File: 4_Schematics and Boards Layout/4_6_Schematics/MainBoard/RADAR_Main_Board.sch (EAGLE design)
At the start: 791 parts, among them IC1 AT93C46A-10SQ-2.7, J1 142-0731-211, J18 142-0731-211, J19 CJT-T-P-HH-ST-TH1, J20 142-0731-211, J21 CJT-T-P-HH-ST-TH1, J22 142-0731-211, J23 142-0731-211, J24 142-0731-211, J25 142-0731-211, J26 142-0731-211, J27 142-0731-211, J28 142-0731-211, J29 142-0731-211, J30 142-0731-211, J31 142-0731-211, J32 142-0731-211, J33 142-0731-211, J34 142-0731-211, J35 142-0731-211, J36 142-0731-211, J37 142-0731-211, J38 142-0731-211, J39 142-0731-211, J40 142-0731-211, J41 142-0731-211, J42 142-0731-211, J43 142-0731-211, J44 142-0731-211, J45 142-0731-211, J46 142-0731-211, J47 142-0731-211, J48 142-0731-211, J49 142-0731-211, J50 142-0731-211, J51 142-0731-211, J52 142-0731-211, J53 142-0731-211, J54 142-0731-211, J55 142-0731-211, U1 AD9484BCPZ-500, U10 ADS7830IPWR, U11 INA241A3IDGKRDGK0008A-MFG, U13 LTC5552IUDBTRMPBF, U14 SZMMSZ5232BT1G, U15 SZMMSZ5232BT1G, U16 EP4RKU+, U17 SZMMSZ5232BT1G, U2 STM32F746ZGT7, U3 AD9708AR, U37 SZMMSZ5232BT1G, U38 SZMMSZ5232BT1G, U39 SZMMSZ5232BT1G, U4 AD8352ACPZ-R7, U40 SZMMSZ5232BT1G, U41 SZMMSZ5232BT1G, U42 XC7A50T-2FTG256I, U43 SZMMSZ5232BT1G, U44 SZMMSZ5232BT1G, U45 SZMMSZ5232BT1G, U46 SZMMSZ5232BT1G, U47 SZMMSZ5232BT1G, U48 SZMMSZ5232BT1G, U49 SZMMSZ5232BT1G, U5 LTC5552IUDBTRMPBF, U50 SZMMSZ5232BT1G, U51 SZMMSZ5232BT1G, U52 SZMMSZ5232BT1G, U53 SZMMSZ5232BT1G, U54 SZMMSZ5232BT1G, U55 SZMMSZ5232BT1G, U56 SZMMSZ5232BT1G, U57 SZMMSZ5232BT1G, U58 SZMMSZ5232BT1G, U59 SZMMSZ5232BT1G, U6 FT2232HQ, U60 SZMMSZ5232BT1G, U61 SZMMSZ5232BT1G, U62 SZMMSZ5232BT1G, U63 SZMMSZ5232BT1G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

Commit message: fix(hw): take the first IF stage from 10 dB to 15 dB (Lane B B1.2)
Stage 1 (`U4`) is set for 10 dB and stage 2 (`U8`) for 15 dB, so the cascade is
25 dB against the ~30 dB the ADC wants. Both stages are AD8352s whose gain comes
from R_G, and the datasheet (Table 5, 200 ohm load) gives 115 ohm for 10 dB and
56 ohm for 15 dB.

Table 5 also pairs each gain with a distortion-cancellation network -- CD of
0.2 pF at 10 dB and 0.6 pF at 15 dB, RD = 4.3k either way -- and stage 2 is built
exactly that way (R22 = 56R, C54 = 0.6pF). So stage 1 needs *two* parts changed,
not one:

    R14  115R  -> 56R      (gain resistor, U4.RGN/U4.RGP)
    C43  0.2pF -> 0.6pF    (CD, with R15 = 4.3k on U4.RDP/U4.RDN)

Changing only R14 would have re-tuned stage 1's distortion cancellation while
claiming a gain change -- the board-respin spec said exactly that, and it is
corrected along with the prefab checklist and the fix plan.

Both replacement part numbers are copied from the stage that already runs at
15 dB in the same BOM, so no MPN was invented:
    RC0201FR-07115RL    -> RC0201FR-0756RL      (as R22)
    GJM0335C1ER20WB01D  -> GJM0335C1ER60WB01D   (as C54)

Applied to the schematic, the board and the production BOM together. Verified:
the CAD files re-parse with identical structure (1978 parts / 744 nets / 2462
segments in the .sch, 791 elements in the .brd), the diff is exactly the four
intended attribute lines, the xlsx round-trip differs in exactly the four
intended cells, and all three artifact gates stay green -- the board/BOM
consistency gate is what proves the three files agree.
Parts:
- C43: value 0.2pF -> 0.6pF
- R14: value 115R -> 56R
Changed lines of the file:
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@@
 <part name="C46" library="eagle-ltspice" deviceset="C" device="C0201" value="0.1uF"/>
 <part name="GND74" library="supply1" deviceset="GND" device=""/>
-<part name="R14" library="rcl" deviceset="R-EU_" device="R0201" value="115R"/>
+<part name="R14" library="rcl" deviceset="R-EU_" device="R0201" value="56R"/>
 <part name="R15" library="rcl" deviceset="R-EU_" device="R0201" value="4.3k"/>
-<part name="C43" library="rcl" deviceset="C-EU" device="C0201" value="0.2pF"/>
+<part name="C43" library="rcl" deviceset="C-EU" device="C0201" value="0.6pF"/>
 <part name="C47" library="eagle-ltspice" deviceset="C" device="C0201" value="0.1uF"/>
 <part name="GND75" library="supply1" deviceset="GND" device=""/>

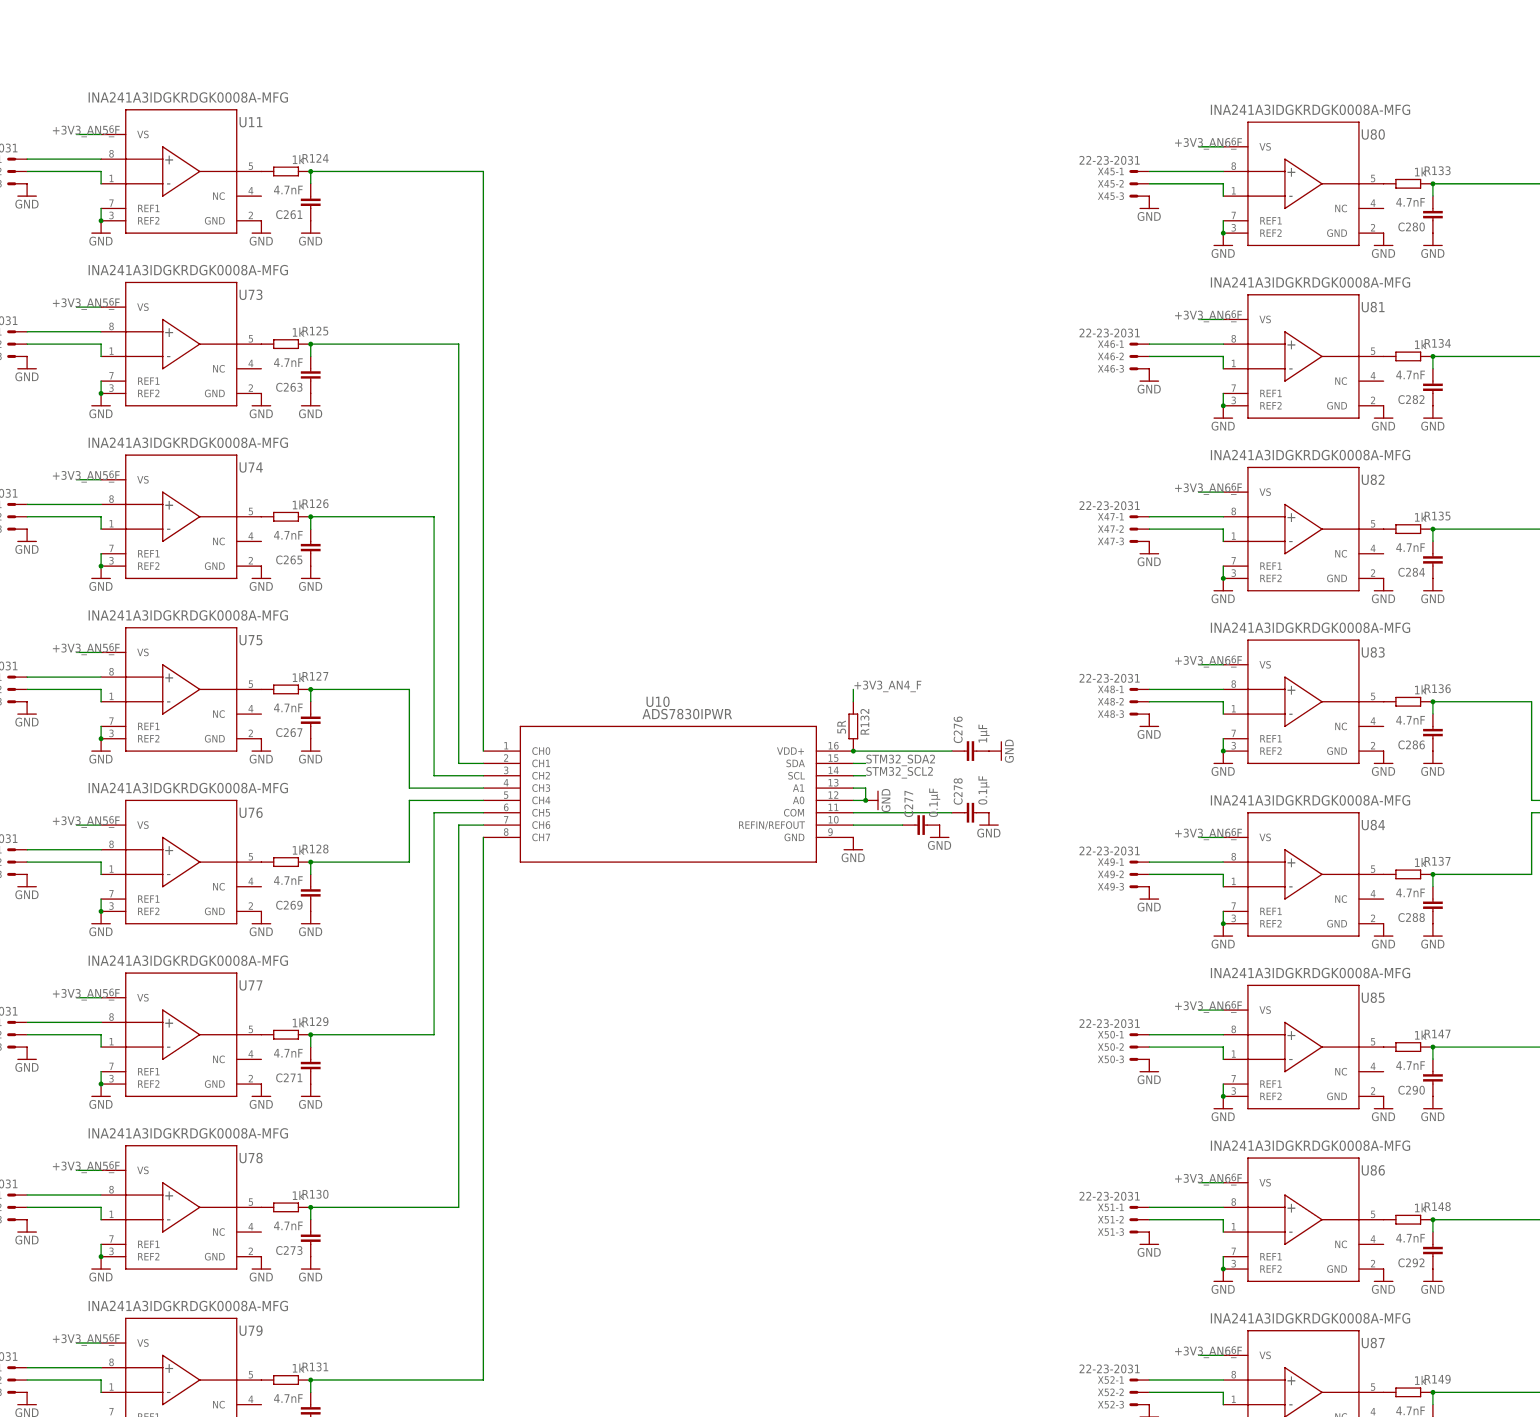
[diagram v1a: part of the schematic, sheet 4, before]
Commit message: fix(hw): move the PA sense chain to the INA241A4 (Lane B B2.5)
The current-sense amplifier is not on the PA board at all -- the shunt (`R10`,
5 mOhm) is, and 16 x `INA241A3IDGKR` on the main board (`U11`, `U73`-`U87`) read
it.  At the A3's 50 V/V into the ADS7830's 2.5 V internal reference the span is
10 A at 39.2 mA/LSB, so the 1.68 A bias target sits at only 17 % of span.

Decision (owner): INA241A4 = 100 V/V.  TI's datasheet lists the gain options as
10/20/50/100/200 V/V for A1/A2/A3/A4/B4, and the A4 shares the A3's DGK/VSSOP-8
package and pinout, so this is a part-number change with no layout impact:

    span         10 A   -> 5 A
    resolution   39.2   -> 19.6 mA/LSB
    1.68 A       17 %   -> 34 % of span      (2.5 A trip still inside 5 A)

Changed together: the schematic (library deviceset *and* the 16 references --
Eagle resolves the symbol from that name, so leaving it at A3 would describe a
different part than the BOM buys), the board's 16 elements, the production BOM
(value, device and MPN) and `PA_INA_GAIN`.  The gain string occurs in three
shapes that share one literal, so the replacement is counted (21 in the .sch,
32 in the .brd) rather than pattern-guessed.

Tests moved to the Rev B chain, including the ones that encoded the superseded
numbers: `test_pa_sense` now expects a 5 A span, 19.6 mA/LSB, target code 86 (was
43) and the 0.1 ohm-shunt diagnostic's 0.25 A full scale; the legacy gap-3
re-read test carried its own copy of the *old* formula (3.3 V reference and gain
50, i.e. the 32 %-low chain Phase 1 replaced), so its local formula and raw
values were brought onto the chain the firmware actually uses.

Verified: CAD structure unchanged (1978 parts / 791 elements), zero stale A3
references, the xlsx differs from HEAD in exactly 3 cells, all three artifact
gates stay green (the board/BOM consistency gate is what proves the three files
agree), MCU suite 26/26 and `test_pa_sense` 6/6.
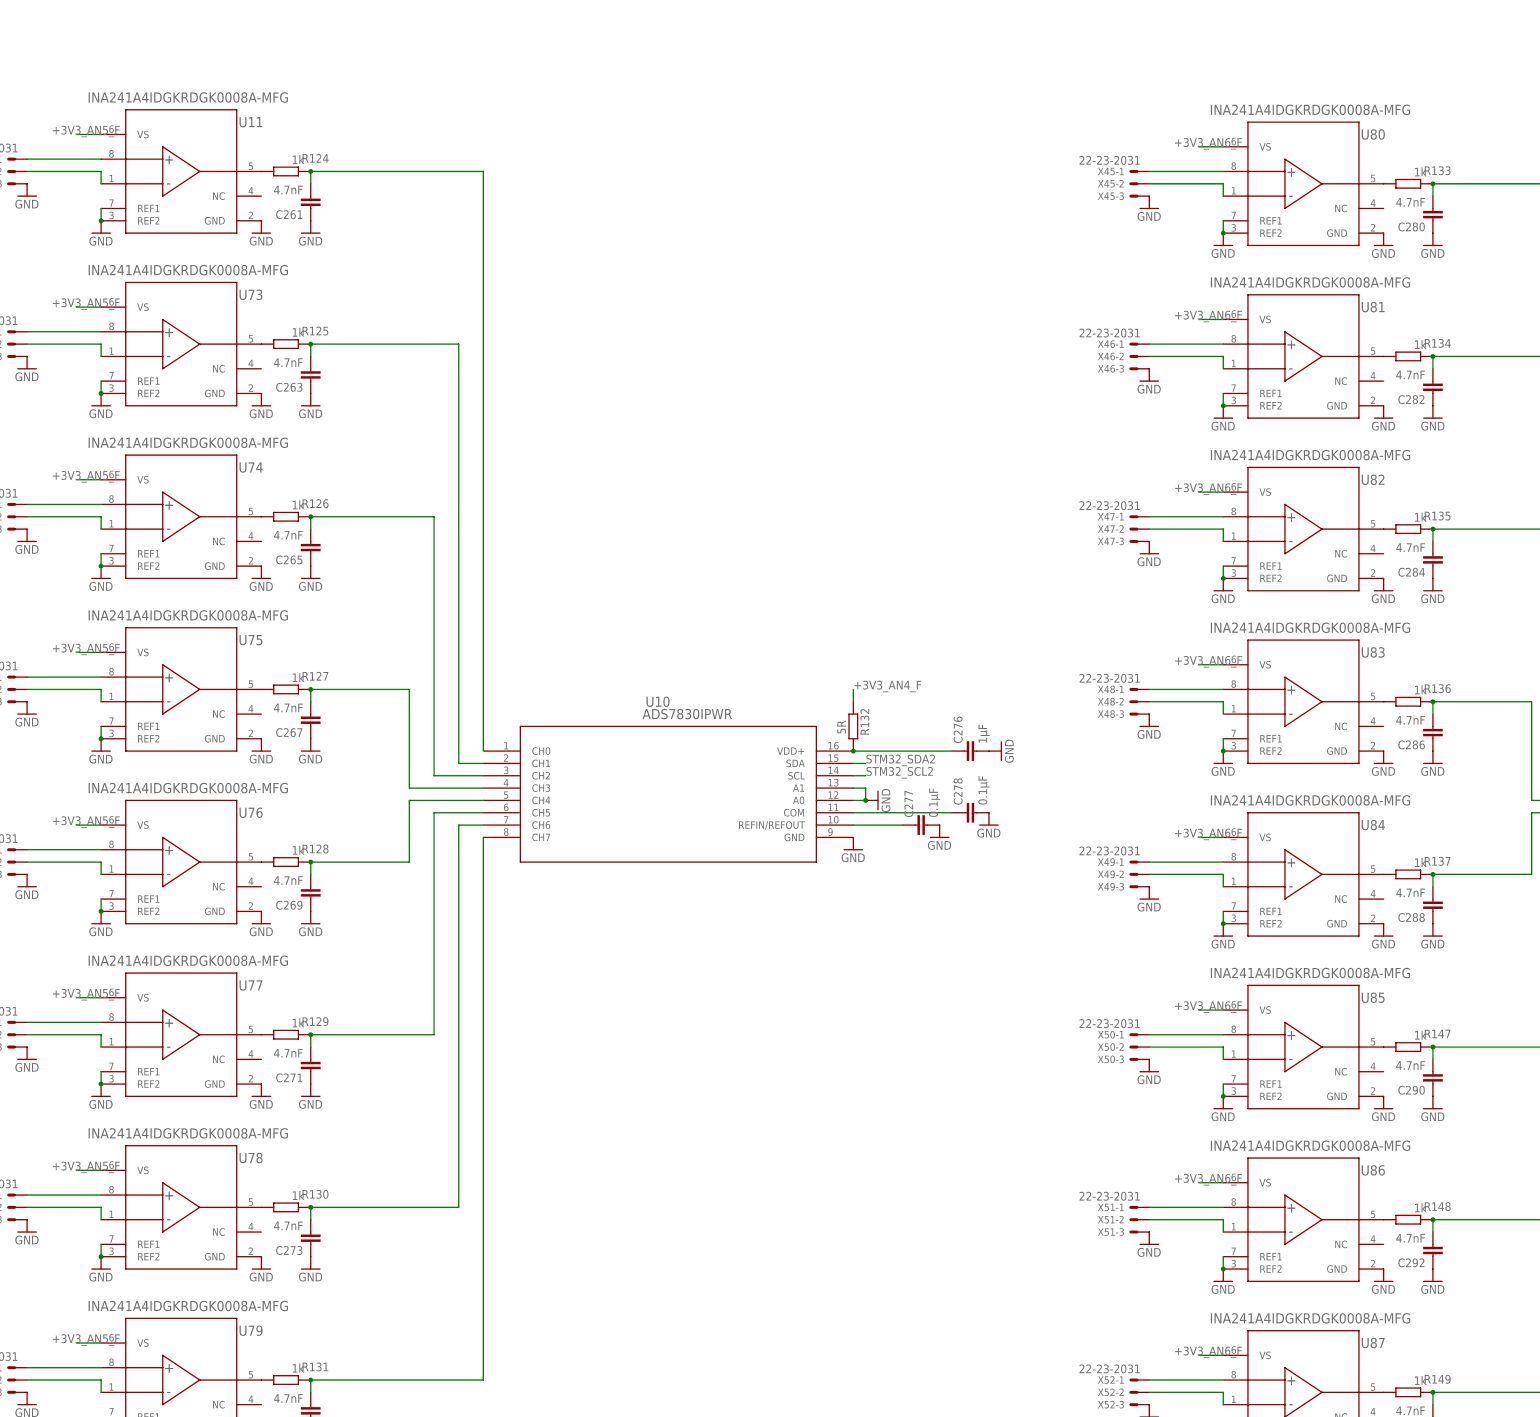
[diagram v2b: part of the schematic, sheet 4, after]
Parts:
- U11, U73, U74, U75, U76, U77, U78, U79, U80, U81, U82, U83, U84, U85, U86, U87: value INA241A3IDGKRDGK0008A-MFG -> INA241A4IDGKRDGK0008A-MFG; device My_Library_RADAR:INA241A3IDGKRDGK0008A-MFG -> My_Library_RADAR:INA241A4IDGKRDGK0008A-MFG
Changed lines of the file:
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@@
 <part name="GND693" library="supply1" deviceset="GND" device=""/>
 <part name="R123" library="eagle-ltspice" deviceset="R" device="R0201" value="10k"/>
-<part name="U80" library="My_Library_RADAR" deviceset="INA241A3IDGKR" device="DGK0008A-MFG"/>
+<part name="U80" library="My_Library_RADAR" deviceset="INA241A4IDGKR" device="DGK0008A-MFG"/>
 <part name="X45" library="con-molex" deviceset="22-23-2031" device=""/>
 <part name="GND1070" library="supply1" deviceset="GND" device=""/>
@@
 <part name="R133" library="eagle-ltspice" deviceset="R" device="R0201" value="1k"/>
 <part name="GND1073" library="supply1" deviceset="GND" device=""/>
-<part name="U81" library="My_Library_RADAR" deviceset="INA241A3IDGKR" device="DGK0008A-MFG"/>
+<part name="U81" library="My_Library_RADAR" deviceset="INA241A4IDGKR" device="DGK0008A-MFG"/>
 <part name="X46" library="con-molex" deviceset="22-23-2031" device=""/>
 <part name="GND1075" library="supply1" deviceset="GND" device=""/>
@@
 <part name="R134" library="eagle-ltspice" deviceset="R" device="R0201" value="1k"/>
 <part name="GND1078" library="supply1" deviceset="GND" device=""/>
-<part name="U82" library="My_Library_RADAR" deviceset="INA241A3IDGKR" device="DGK0008A-MFG"/>
+<part name="U82" library="My_Library_RADAR" deviceset="INA241A4IDGKR" device="DGK0008A-MFG"/>
 <part name="X47" library="con-molex" deviceset="22-23-2031" device=""/>
 <part name="GND1080" library="supply1" deviceset="GND" device=""/>
@@
 <part name="R135" library="eagle-ltspice" deviceset="R" device="R0201" value="1k"/>
 <part name="GND1083" library="supply1" deviceset="GND" device=""/>
-<part name="U83" library="My_Library_RADAR" deviceset="INA241A3IDGKR" device="DGK0008A-MFG"/>
+<part name="U83" library="My_Library_RADAR" deviceset="INA241A4IDGKR" device="DGK0008A-MFG"/>
 <part name="X48" library="con-molex" deviceset="22-23-2031" device=""/>
 <part name="GND1085" library="supply1" deviceset="GND" device=""/>
@@
 <part name="R136" library="eagle-ltspice" deviceset="R" device="R0201" value="1k"/>
 <part name="GND1088" library="supply1" deviceset="GND" device=""/>
-<part name="U84" library="My_Library_RADAR" deviceset="INA241A3IDGKR" device="DGK0008A-MFG"/>
+<part name="U84" library="My_Library_RADAR" deviceset="INA241A4IDGKR" device="DGK0008A-MFG"/>
 <part name="X49" library="con-molex" deviceset="22-23-2031" device=""/>
 <part name="GND1090" library="supply1" deviceset="GND" device=""/>
@@
 <part name="R137" library="eagle-ltspice" deviceset="R" device="R0201" value="1k"/>
 <part name="GND1093" library="supply1" deviceset="GND" device=""/>
-<part name="U85" library="My_Library_RADAR" deviceset="INA241A3IDGKR" device="DGK0008A-MFG"/>
+<part name="U85" library="My_Library_RADAR" deviceset="INA241A4IDGKR" device="DGK0008A-MFG"/>
 <part name="X50" library="con-molex" deviceset="22-23-2031" device=""/>
 <part name="GND1095" library="supply1" deviceset="GND" device=""/>
@@
 <part name="R147" library="eagle-ltspice" deviceset="R" device="R0201" value="1k"/>
 <part name="GND1098" library="supply1" deviceset="GND" device=""/>
-<part name="U86" library="My_Library_RADAR" deviceset="INA241A3IDGKR" device="DGK0008A-MFG"/>
+<part name="U86" library="My_Library_RADAR" deviceset="INA241A4IDGKR" device="DGK0008A-MFG"/>
 <part name="X51" library="con-molex" deviceset="22-23-2031" device=""/>
 <part name="GND1100" library="supply1" deviceset="GND" device=""/>
@@
 <part name="R148" library="eagle-ltspice" deviceset="R" device="R0201" value="1k"/>
 <part name="GND1103" library="supply1" deviceset="GND" device=""/>
-<part name="U87" library="My_Library_RADAR" deviceset="INA241A3IDGKR" device="DGK0008A-MFG"/>
+<part name="U87" library="My_Library_RADAR" deviceset="INA241A4IDGKR" device="DGK0008A-MFG"/>
 <part name="X52" library="con-molex" deviceset="22-23-2031" device=""/>
 <part name="GND1105" library="supply1" deviceset="GND" device=""/>
@@
 <part name="C350" library="rcl" deviceset="C-EU" device="C0402" value="100nF"/>
 <part name="C351" library="rcl" deviceset="C-EU" device="C0402" value="100nF"/>
-<part name="U11" library="My_Library_RADAR" deviceset="INA241A3IDGKR" device="DGK0008A-MFG"/>
+<part name="U11" library="My_Library_RADAR" deviceset="INA241A4IDGKR" device="DGK0008A-MFG"/>
 <part name="X3" library="con-molex" deviceset="22-23-2031" device=""/>
 <part name="GND1025" library="supply1" deviceset="GND" device=""/>
@@
 <part name="R124" library="eagle-ltspice" deviceset="R" device="R0201" value="1k"/>
 <part name="GND1028" library="supply1" deviceset="GND" device=""/>
-<part name="U73" library="My_Library_RADAR" deviceset="INA241A3IDGKR" device="DGK0008A-MFG"/>
+<part name="U73" library="My_Library_RADAR" deviceset="INA241A4IDGKR" device="DGK0008A-MFG"/>
 <part name="X38" library="con-molex" deviceset="22-23-2031" device=""/>
 <part name="GND1030" library="supply1" deviceset="GND" device=""/>
@@
 <part name="R125" library="eagle-ltspice" deviceset="R" device="R0201" value="1k"/>
 <part name="GND1033" library="supply1" deviceset="GND" device=""/>
-<part name="U74" library="My_Library_RADAR" deviceset="INA241A3IDGKR" device="DGK0008A-MFG"/>
+<part name="U74" library="My_Library_RADAR" deviceset="INA241A4IDGKR" device="DGK0008A-MFG"/>
 <part name="X39" library="con-molex" deviceset="22-23-2031" device=""/>
 <part name="GND1035" library="supply1" deviceset="GND" device=""/>
@@
 <part name="R126" library="eagle-ltspice" deviceset="R" device="R0201" value="1k"/>
 <part name="GND1038" library="supply1" deviceset="GND" device=""/>
-<part name="U75" library="My_Library_RADAR" deviceset="INA241A3IDGKR" device="DGK0008A-MFG"/>
+<part name="U75" library="My_Library_RADAR" deviceset="INA241A4IDGKR" device="DGK0008A-MFG"/>
 <part name="X40" library="con-molex" deviceset="22-23-2031" device=""/>
 <part name="GND1040" library="supply1" deviceset="GND" device=""/>
@@
 <part name="R127" library="eagle-ltspice" deviceset="R" device="R0201" value="1k"/>
 <part name="GND1043" library="supply1" deviceset="GND" device=""/>
-<part name="U76" library="My_Library_RADAR" deviceset="INA241A3IDGKR" device="DGK0008A-MFG"/>
+<part name="U76" library="My_Library_RADAR" deviceset="INA241A4IDGKR" device="DGK0008A-MFG"/>
 <part name="X41" library="con-molex" deviceset="22-23-2031" device=""/>
 <part name="GND1045" library="supply1" deviceset="GND" device=""/>
@@
 <part name="R128" library="eagle-ltspice" deviceset="R" device="R0201" value="1k"/>
 <part name="GND1048" library="supply1" deviceset="GND" device=""/>
-<part name="U77" library="My_Library_RADAR" deviceset="INA241A3IDGKR" device="DGK0008A-MFG"/>
+<part name="U77" library="My_Library_RADAR" deviceset="INA241A4IDGKR" device="DGK0008A-MFG"/>
 <part name="X42" library="con-molex" deviceset="22-23-2031" device=""/>
 <part name="GND1050" library="supply1" deviceset="GND" device=""/>
@@
 <part name="R129" library="eagle-ltspice" deviceset="R" device="R0201" value="1k"/>
 <part name="GND1053" library="supply1" deviceset="GND" device=""/>
-<part name="U78" library="My_Library_RADAR" deviceset="INA241A3IDGKR" device="DGK0008A-MFG"/>
+<part name="U78" library="My_Library_RADAR" deviceset="INA241A4IDGKR" device="DGK0008A-MFG"/>
 <part name="X43" library="con-molex" deviceset="22-23-2031" device=""/>
 <part name="GND1055" library="supply1" deviceset="GND" device=""/>
@@
 <part name="R130" library="eagle-ltspice" deviceset="R" device="R0201" value="1k"/>
 <part name="GND1058" library="supply1" deviceset="GND" device=""/>
-<part name="U79" library="My_Library_RADAR" deviceset="INA241A3IDGKR" device="DGK0008A-MFG"/>
+<part name="U79" library="My_Library_RADAR" deviceset="INA241A4IDGKR" device="DGK0008A-MFG"/>
 <part name="X44" library="con-molex" deviceset="22-23-2031" device=""/>
 <part name="GND1060" library="supply1" deviceset="GND" device=""/>
